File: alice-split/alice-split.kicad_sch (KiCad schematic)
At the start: 137 parts, among them J1 MJ-4PP-9-Lily58-cache-Lily58_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, SW1 RotaryEncoder_Switch, SW38 SW_PUSH-MX_W_LED, SW41 SW_PUSH-MX_W_LED, SW42 SW_PUSH-MX_W_LED, SW43 SW_PUSH-MX_W_LED, SW44 SW_PUSH-MX_W_LED, SW45 SW_PUSH-MX_W_LED, SW46 SW_PUSH-MX_W_LED, SW47 SW_PUSH-MX_W_LED, SW48 SW_PUSH-MX_W_LED, SW49 SW_PUSH-MX_W_LED, SW50 SW_PUSH-MX_W_LED, SW51 SW_PUSH-MX_W_LED, SW52 SW_PUSH-MX_W_LED, SW53 SW_PUSH-MX_W_LED, SW54 SW_PUSH-MX_W_LED, SW55 SW_PUSH-MX_W_LED, SW56 SW_PUSH-MX_W_LED, SW57 SW_PUSH-MX_W_LED, SW58 SW_PUSH-MX_W_LED, SW59 SW_PUSH-MX_W_LED, SW60 SW_PUSH-MX_W_LED, SW61 SW_PUSH-MX_W_LED, SW62 SW_PUSH-MX_W_LED, SW63 SW_PUSH-MX_W_LED, SW64 SW_PUSH-MX_W_LED, SW65 SW_PUSH-MX_W_LED, SW66 SW_PUSH-MX_W_LED, SW67 SW_PUSH-MX_W_LED, SW68 SW_PUSH-MX_W_LED, SW69 SW_PUSH-MX_W_LED, SW70 SW_PUSH-MX_W_LED, SW71 SW_PUSH-MX_W_LED, SW72 SW_PUSH-MX_W_LED, SW73 SW_PUSH-MX_W_LED, SW74 SW_PUSH-MX_W_LED, SW75 SW_PUSH-MX_W_LED, SW76 SW_PUSH-MX_W_LED, SW77 SW_PUSH-MX_W_LED, SW78 SW_PUSH-MX_W_LED, SW79 SW_PUSH-MX_W_LED, SW80 SW_PUSH-MX_W_LED, SW81 SW_PUSH-MX_W_LED, SW82 SW_PUSH-MX_W_LED, SW83 SW_PUSH-MX_W_LED, SW84 SW_PUSH-MX_W_LED, SW85 SW_PUSH-MX_W_LED, SW86 SW_PUSH-MX_W_LED, SW87 SW_PUSH-MX_W_LED, SW88 SW_PUSH-MX_W_LED, SW89 SW_PUSH-MX_W_LED, U1 Sparkfun_Pro_Micro

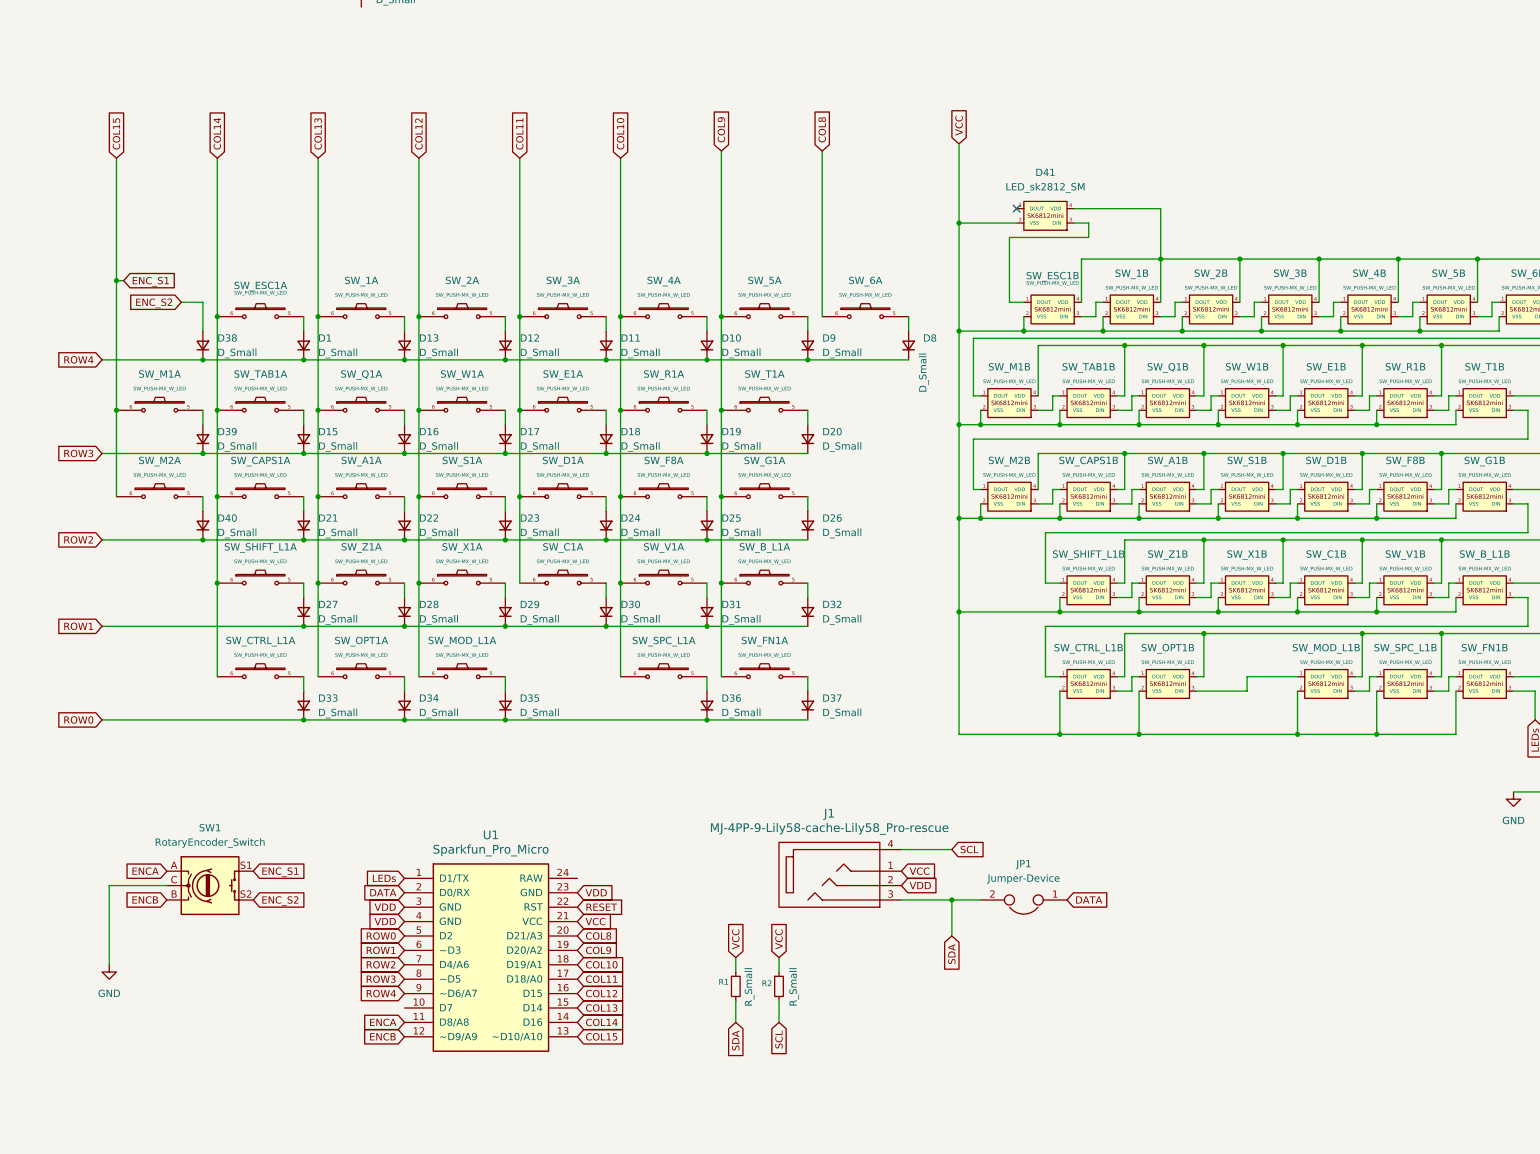
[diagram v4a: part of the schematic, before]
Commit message: Wired the TRRS connector. Updated a few other things too.
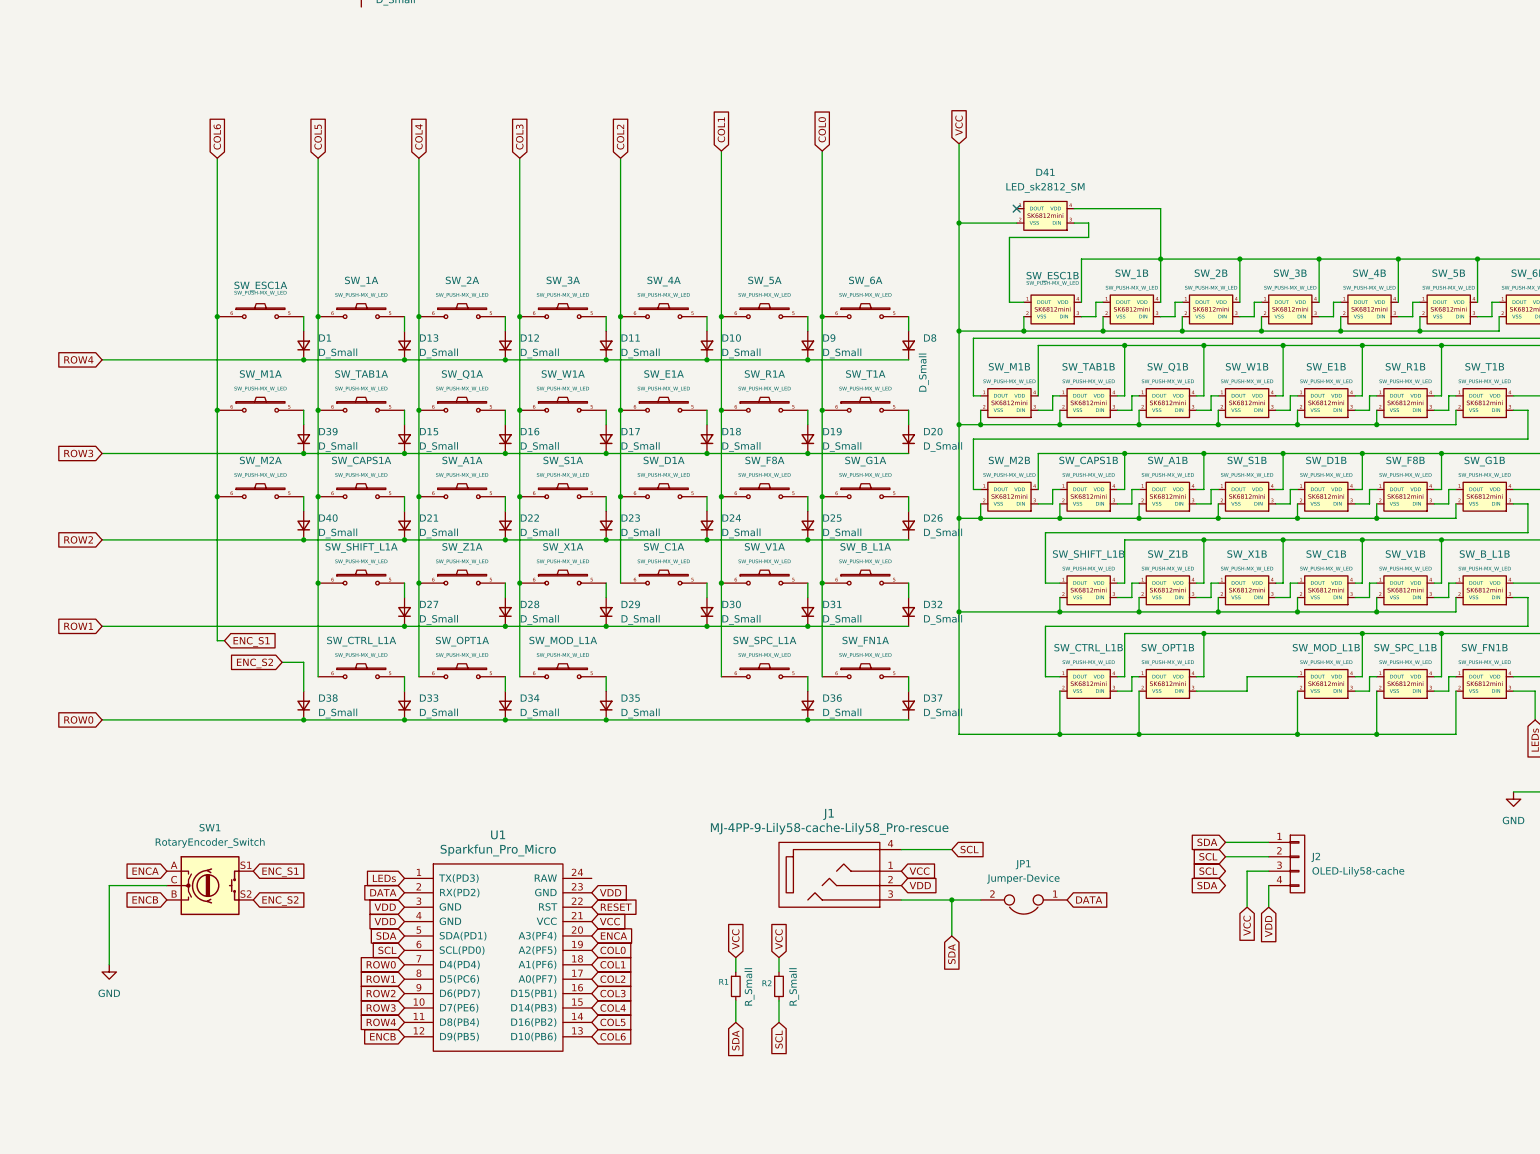
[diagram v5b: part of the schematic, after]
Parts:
- added J2: OLED-Lily58-cache, SofleKeyboard-footprint:OLED_4Pin, symbol SofleKeyboard-rescue:OLED-Lily58-cache
- J1: footprint SofleRGB:MJ-4PP-9 -> SofleKeyboard-footprint:MJ-4PP-9
- JP1: footprint SofleRGB:jumper_data -> SofleRGB:Jumper
- U1: symbol Arduino:Sparkfun_Pro_Micro -> SofleKeyboard-rescue:ProMicro_2-Lily58-cache-Lily58_Pro-rescue
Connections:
- net ENCA: now also U1.20 (A3(PF4)); no longer U1.11 (D8/A8)
- net GND: now also J2.4 (P4)
- net ROW0: now also D38.1 (K), U1.7 (D4(PD4)); no longer U1.5 (D2)
- net ROW1: now also U1.8 (D5(PC6)); no longer U1.6 (~D3)
- net ROW2: now also U1.9 (D6(PD7)); no longer U1.7 (D4/A6)
- net ROW3: now also U1.10 (D7(PE6)); no longer U1.8 (~D5)
- net ROW4: now also U1.11 (D8(PB4)); no longer D38.1 (K), U1.9 (~D6/A7)
- net SCL: now also U1.6 (SCL(PD0)), J2.2 (P2)
- net SDA: now also U1.5 (SDA(PD1)), J2.1 (P1)
- net VCC: now also J2.3 (P3)
- net COL10 renamed COL1
- net COL1: now also SW_5.6; no longer SW_4.6
- net COL11 renamed COL2
- net COL2: now also SW_4.6; no longer SW_3.6
- net COL12 renamed COL3
- net COL3: now also SW_3.6; no longer SW_2.6
- net COL13 renamed COL4
- net COL4: now also SW_2.6; no longer SW_1.6
- net COL14 renamed COL5
- net COL5: now also SW_1.6; no longer SW_ESC1.6
- net COL15 renamed COL6
- net COL6: now also SW_ESC1.6
- net COL8 renamed COL0
- net COL0: now also SW_B_L1.6, SW_FN1.6, SW_G1.6, SW_T1.6, U1.19 (A2(PF5)); no longer U1.20 (D21/A3)
- removed net COL9: SW_5.6, SW_B_L1.6, SW_FN1.6, SW_G1.6, SW_T1.6, U1.19 (D20/A2)
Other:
- moved on the sheet: D15, D16, D17, D18, D19, D20, D21, D22, D23, D24, D25, D26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

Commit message: Started working on the right half of the keyboard.
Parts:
- removed SW38, SW41, SW42, SW43, SW44, SW45, SW46, SW47, SW48, SW49, SW50, SW51, SW52, SW53, SW54, SW55, SW56, SW57, SW58, SW59, SW60, SW61, SW62, SW63, SW64, SW65, SW66, SW67, SW68, SW69, SW70, SW71, SW72, SW73, SW74, SW75, SW76, SW77, SW78, SW79, SW80, SW81, SW82, SW83, SW84, SW85, SW86, SW87, SW88, SW89: SW_PUSH-MX_W_LED, SofleRGB:SK6812MINI_and_cherry, symbol SofleKeyboard:SW_PUSH-MX_W_LED
- removed unit 1 of SW_M1
- renumbered D41 to D_ENC_L1, SW1 to SW_ENC_L1
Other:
- added sheet Right Hand Side (right-hand-side.kicad_sch)

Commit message: Added vias. Finished bottom side for now. Started working on the topside.
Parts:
- added unit 1 of SW_MACRO1
- renumbered SW_M1 to SW_MACRO1, SW_M2 to SW_MACRO2
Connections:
- net COL0: now also U1.13 (D10(PB6)); no longer U1.19 (A2(PF5))
- net COL1: now also U1.12 (D9(PB5)); no longer U1.18 (A1(PF6))
- net COL2: now also U1.11 (D8(PB4)); no longer U1.17 (A0(PF7))
- net COL3: now also U1.10 (D7(PE6)); no longer U1.16 (D15(PB1))
- net COL4: now also U1.9 (D6(PD7)); no longer U1.15 (D14(PB3))
- net COL5: now also U1.8 (D5(PC6)); no longer U1.14 (D16(PB2))
- net COL6: now also U1.7 (D4(PD4)), SW_MACRO1.6; no longer U1.13 (D10(PB6))
- net ENCB: now also U1.19 (A2(PF5)); no longer U1.12 (D9(PB5))
- net ROW0: now also U1.14 (D16(PB2)); no longer U1.7 (D4(PD4))
- net ROW1: now also U1.15 (D14(PB3)); no longer U1.8 (D5(PC6))
- net ROW2: now also U1.16 (D15(PB1)); no longer U1.9 (D6(PD7))
- net ROW3: now also U1.17 (A0(PF7)); no longer U1.10 (D7(PE6))
- net ROW4: now also U1.18 (A1(PF6)); no longer U1.11 (D8(PB4))
- net at D39.2 (A): now also SW_MACRO1.5
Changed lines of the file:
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@@
 	)
 	(junction
+		(at 41.91 68.58)
+		(diameter 0)
+		(color 0 0 0 0)
+	)
+	(junction
 		(at 95.25 99.06)
 		(diameter 0)
@@
 	(wire
 		(pts
-			(xy 41.91 52.07) (xy 41.91 83.82)
+			(xy 41.91 52.07) (xy 41.91 68.58)
 		)
 		(stroke
@@
 	(wire
 		(pts
+			(xy 41.91 68.58) (xy 41.91 83.82)
+		)
+		(stroke
+			(width 0)
+			(type default)
+		)
+	)
+	(wire
+		(pts
 			(xy 280.67 41.91) (xy 280.67 49.53)
 		)
@@
 	(hierarchical_label "ROW4"
 		(shape input)
-		(at 74.93 176.53 180)
+		(at 107.95 166.37 0)
 		(effects
 			(font
 				(size 1.27 1.27)
 			)
-			(justify right)
+			(justify left)
 		)
 	)
 	(hierarchical_label "COL4"
 		(shape input)
-		(at 107.95 173.99 0)
+		(at 74.93 171.45 180)
 		(effects
 			(font
 				(size 1.27 1.27)
 			)
-			(justify left)
+			(justify right)
 		)
 	)
@@
 	(hierarchical_label "COL5"
 		(shape input)
-		(at 107.95 176.53 0)
+		(at 74.93 168.91 180)
 		(effects
 			(font
 				(size 1.27 1.27)
 			)
-			(justify left)
+			(justify right)
 		)
 	)
@@
 	(hierarchical_label "ROW0"
 		(shape input)
-		(at 74.93 166.37 180)
+		(at 107.95 176.53 0)
 		(effects
 			(font
 				(size 1.27 1.27)
 			)
-			(justify right)
+			(justify left)
 		)
 	)
@@
 	(hierarchical_label "COL1"
 		(shape input)
-		(at 107.95 166.37 0)
+		(at 74.93 179.07 180)
 		(effects
 			(font
 				(size 1.27 1.27)
 			)
-			(justify left)
+			(justify right)
 		)
 	)
@@
 	(hierarchical_label "ROW2"
 		(shape input)
-		(at 74.93 171.45 180)
+		(at 107.95 171.45 0)
 		(effects
 			(font
 				(size 1.27 1.27)
 			)
-			(justify right)
+			(justify left)
 		)
 	)
@@
 	(hierarchical_label "ROW3"
 		(shape input)
-		(at 74.93 173.99 180)
+		(at 107.95 168.91 0)
 		(effects
 			(font
 				(size 1.27 1.27)
 			)
-			(justify right)
+			(justify left)
 		)
 	)
 	(hierarchical_label "ROW1"
 		(shape input)
-		(at 74.93 168.91 180)
+		(at 107.95 173.99 0)
 		(effects
 			(font
 				(size 1.27 1.27)
 			)
-			(justify right)
+			(justify left)
 		)
 	)
@@
 	(hierarchical_label "COL3"
 		(shape input)
-		(at 107.95 171.45 0)
+		(at 74.93 173.99 180)
 		(effects
 			(font
 				(size 1.27 1.27)
 			)
-			(justify left)
+			(justify right)
 		)
 	)
 	(hierarchical_label "ENCB"
 		(shape input)
-		(at 74.93 179.07 180)
+		(at 107.95 163.83 0)
 		(effects
 			(font
 				(size 1.27 1.27)
 			)
-			(justify right)
+			(justify left)
 		)
 	)
 	(hierarchical_label "COL2"
 		(shape input)
-		(at 107.95 168.91 0)
+		(at 74.93 176.53 180)
 		(effects
 			(font
 				(size 1.27 1.27)
 			)
-			(justify left)
+			(justify right)
 		)
 	)
@@
 	(hierarchical_label "COL6"
 		(shape input)
-		(at 107.95 179.07 0)
+		(at 74.93 166.37 180)
 		(effects
 			(font
 				(size 1.27 1.27)
 			)
-			(justify left)
+			(justify right)
 		)
 	)
 	(hierarchical_label "COL0"
 		(shape input)
-		(at 107.95 163.83 0)
+		(at 107.95 179.07 0)
 		(effects
 			(font
@@
 		(dnp no)
 		(fields_autoplaced yes)
-		(property "Reference" "SW_M1"
+		(property "Reference" "SW_MACRO1"
 			(at 181.61 60.96 0)
 			(effects
@@
 			(project ""
 				(path "/bb4d8238-ce23-40f3-a858-bd67b0639c88"
-					(reference "SW_M1")
+					(reference "SW_MACRO1")
 					(unit 2)
 				)
@@
 		(dnp no)
 		(fields_autoplaced yes)
-		(property "Reference" "SW_M2"
+		(property "Reference" "SW_MACRO2"
 			(at 49.53 77.47 0)
 			(effects
@@
 			(project ""
 				(path "/bb4d8238-ce23-40f3-a858-bd67b0639c88"
-					(reference "SW_M2")
+					(reference "SW_MACRO2")
 					(unit 1)
 				)
@@
 	)
 	(symbol
+		(lib_id "SofleKeyboard:SW_PUSH-MX_W_LED")
+		(at 49.53 68.58 0)
+		(unit 1)
+		(exclude_from_sim no)
+		(in_bom yes)
+		(on_board yes)
+		(dnp no)
+		(fields_autoplaced yes)
+		(property "Reference" "SW_MACRO1"
+			(at 49.53 62.23 0)
+			(effects
+				(font
+					(size 1.27 1.27)
+				)
+			)
+		)
+		(property "Value" "SW_PUSH-MX_W_LED"
+			(at 49.53 64.77 0)
+			(effects
+				(font
+					(size 0.635 0.635)
+				)
+			)
+		)
+		(property "Footprint" "SofleRGB:SK6812MINI_and_cherry"
+			(at 49.53 64.77 0)
+			(effects
+				(font
+					(size 1.27 1.27)
+				)
+				(hide yes)
+			)
+		)
+		(property "Datasheet" ""
+			(at 49.53 64.77 0)
+			(effects
+				(font
+					(size 1.27 1.27)
+				)
+				(hide yes)
+			)
+		)
+		(property "Description" ""
+			(at 49.53 68.58 0)
+			(effects
+				(font
+					(size 1.27 1.27)
+				)
+				(hide yes)
+			)
+		)
+		(pin "4"
+		)
+		(pin "3"
+		)
+		(pin "6"
+		)
+		(pin "5"
+		)
+		(pin "1"
+		)
+		(pin "2"
+		)
+		(instances
+			(project "alice-split"
+				(path "/bb4d8238-ce23-40f3-a858-bd67b0639c88"
+					(reference "SW_MACRO1")
+					(unit 1)
+				)
+			)
+		)
+	)
+	(symbol
 		(lib_id "power:GND")
 		(at 22.86 166.37 0)
@@
 		(on_board yes)
 		(dnp no)
-		(property "Reference" "SW_M2"
+		(property "Reference" "SW_MACRO2"
 			(at 181.61 77.47 0)
 			(effects
@@
 			(project ""
 				(path "/bb4d8238-ce23-40f3-a858-bd67b0639c88"
-					(reference "SW_M2")
+					(reference "SW_MACRO2")
 					(unit 2)
 				)
